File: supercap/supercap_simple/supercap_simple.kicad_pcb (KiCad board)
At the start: 4 copper layers, 84 x 145.5 mm, 54 parts, among them J1 Conn_01x02, J2 Conn_01x02, J4 Conn_01x02, J5 Conn_01x02

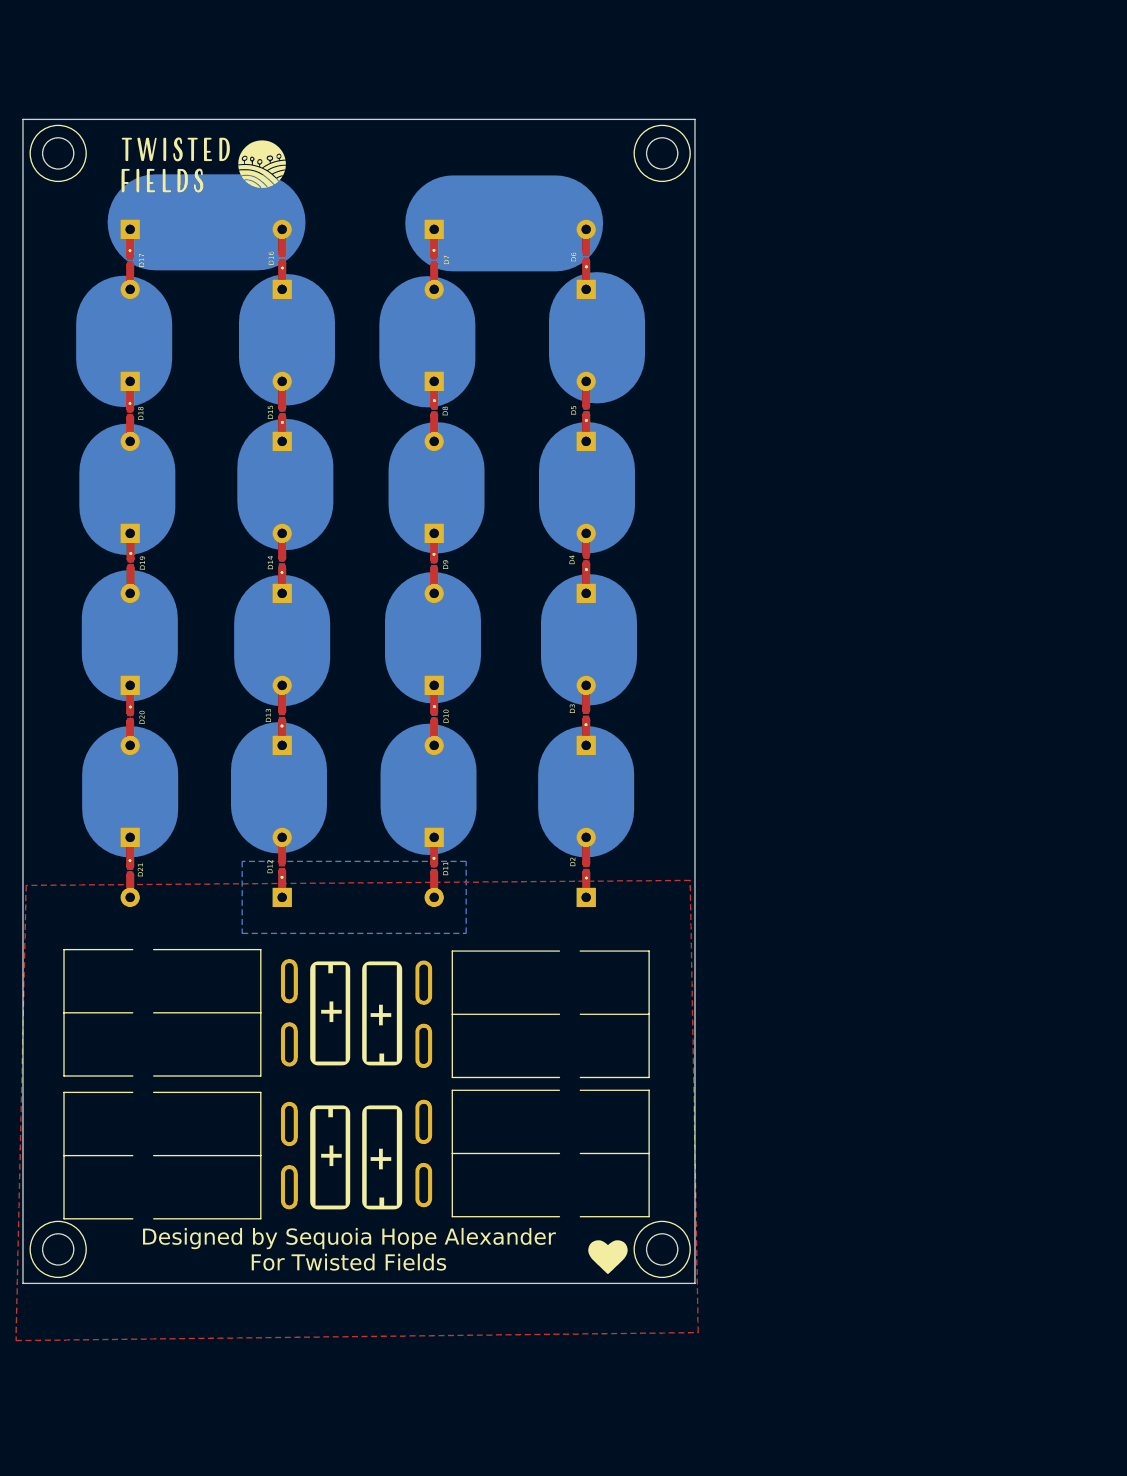
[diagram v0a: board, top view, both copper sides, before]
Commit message: Updated board files for July 2024 order. Added supercap_simple.
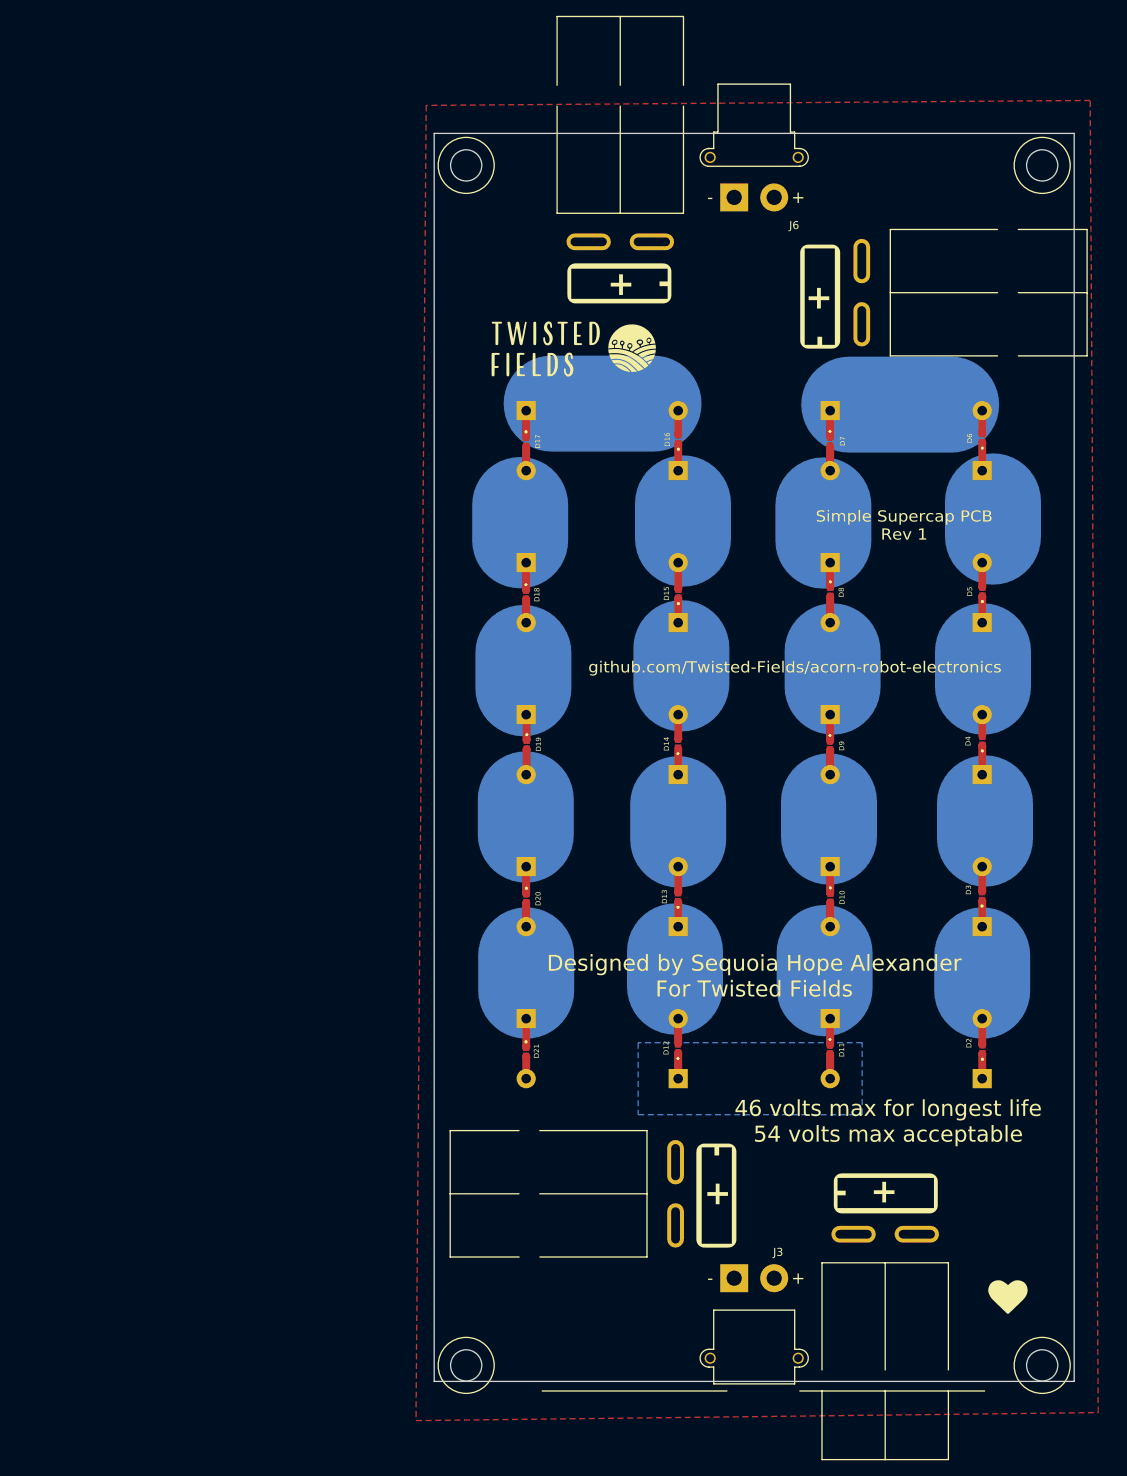
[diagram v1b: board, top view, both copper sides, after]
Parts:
- added J3: XT30PW-M, Connector_AMASS:AMASS_XT30PW-M_1x02_P2.50mm_Horizontal, F.Cu at (147.5, 165.1)
- added J6: XT30PW-F20.G.Y, Connector_AMASS:AMASS_XT30PW-F_1x02_P2.50mm_Horizontal, F.Cu at (147.5, 30.0)
- moved J4 120.7 mm to (163.4, 38.0)
- moved J5 94.9 mm to (129.3, 35.6), turned to 0 degrees
- moved J2 81.9 mm to (170.3, 159.6), turned to 180 degrees
- moved C10 54.4 mm to (159.5, 56.7)
- moved C11 54.4 mm to (159.5, 75.7)
- moved C12 54.4 mm to (159.5, 94.7)
- moved C13 54.4 mm to (159.5, 113.7)
- moved C17 54.4 mm to (159.5, 132.7)
- moved C18 54.4 mm to (140.5, 140.2)
- moved C19 54.4 mm to (140.5, 121.2)
- moved C20 54.4 mm to (140.5, 102.2)
- moved C21 54.4 mm to (140.5, 83.2)
- moved C22 54.4 mm to (140.5, 64.2)
- moved C23 54.4 mm to (121.5, 56.7)
- moved C24 54.4 mm to (121.5, 75.7)
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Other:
- board size 84 x 145.5 mm -> 80 x 156 mm
- board text added: "46 volts max for longest life 54 volts max acceptable"
- board text added: "Simple Supercap PCB Rev 1"
- board text added: "github.com/Twisted-Fields/acorn-robot-electronics"
- board text removed: "github.com/Twisted-Fields/rp2040-motor-controller"
